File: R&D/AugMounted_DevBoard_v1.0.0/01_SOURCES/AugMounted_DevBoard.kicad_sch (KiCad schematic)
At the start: 0 parts

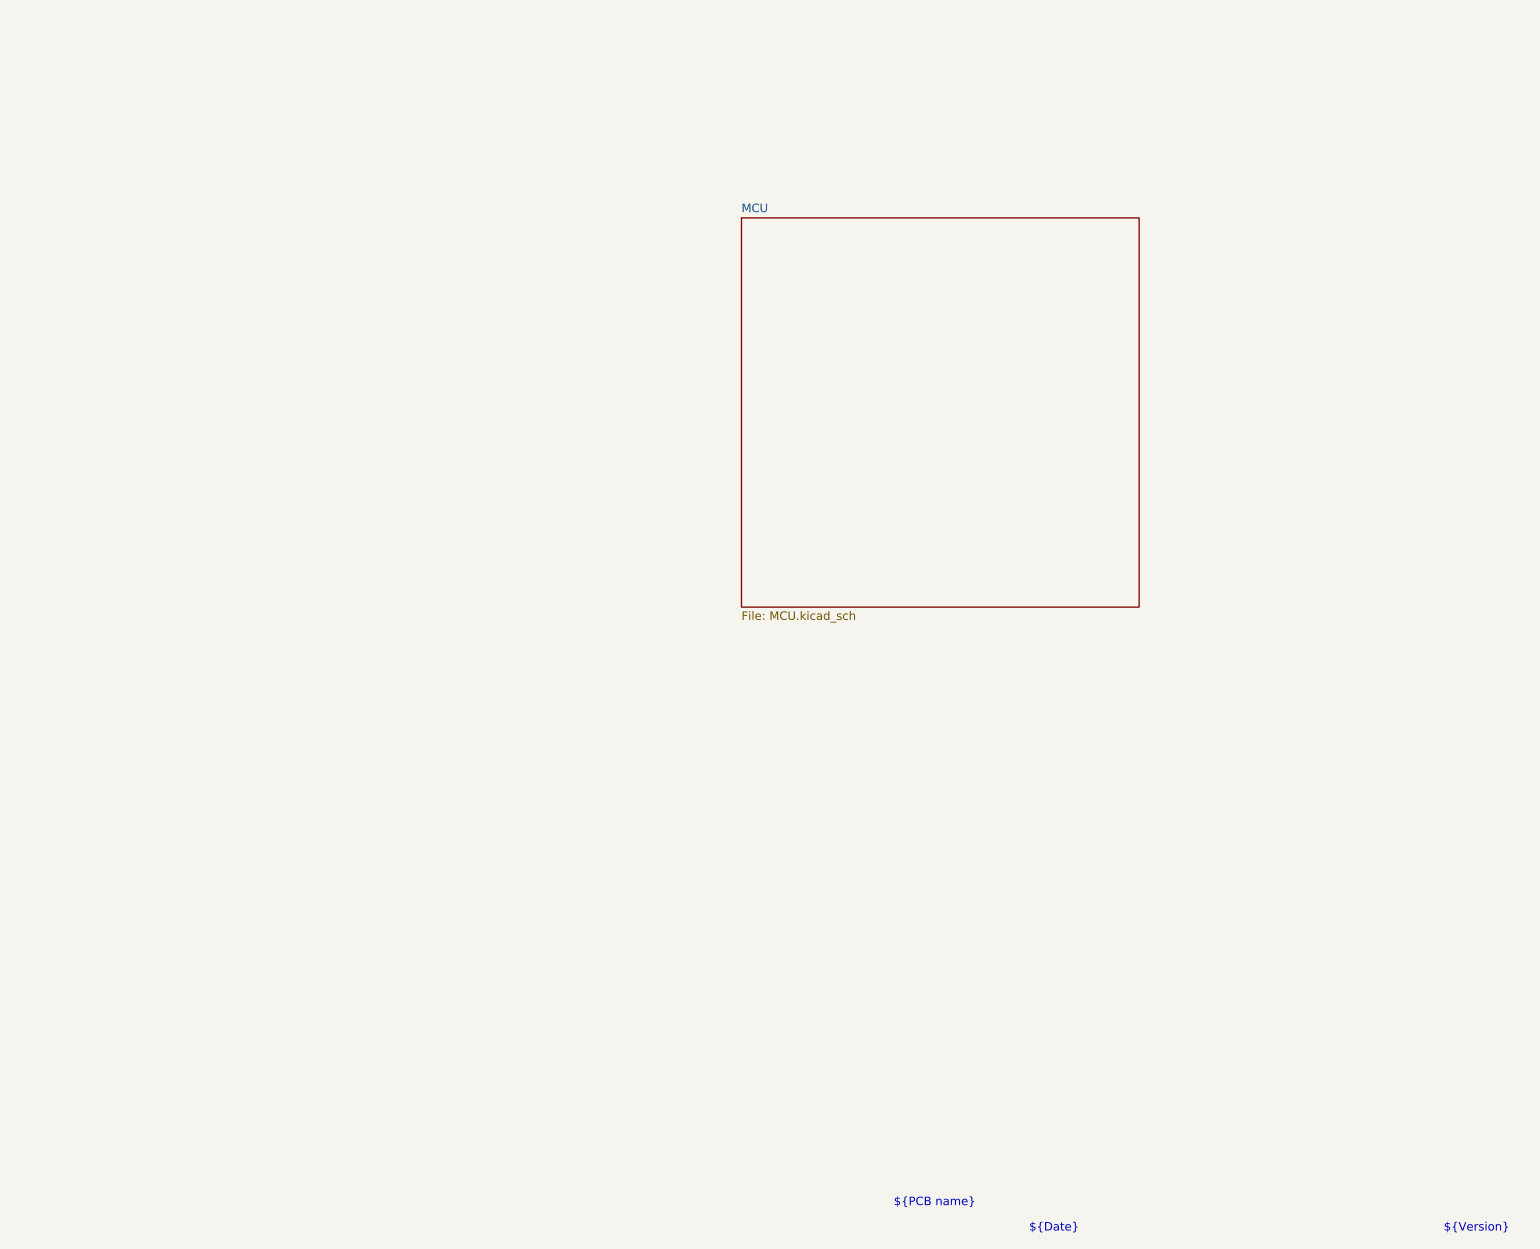
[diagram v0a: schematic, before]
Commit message: Created all components, placed them, and added images of typical applications. ECX334A and ESP32-S3 pdf are available in 00_RESOURCES
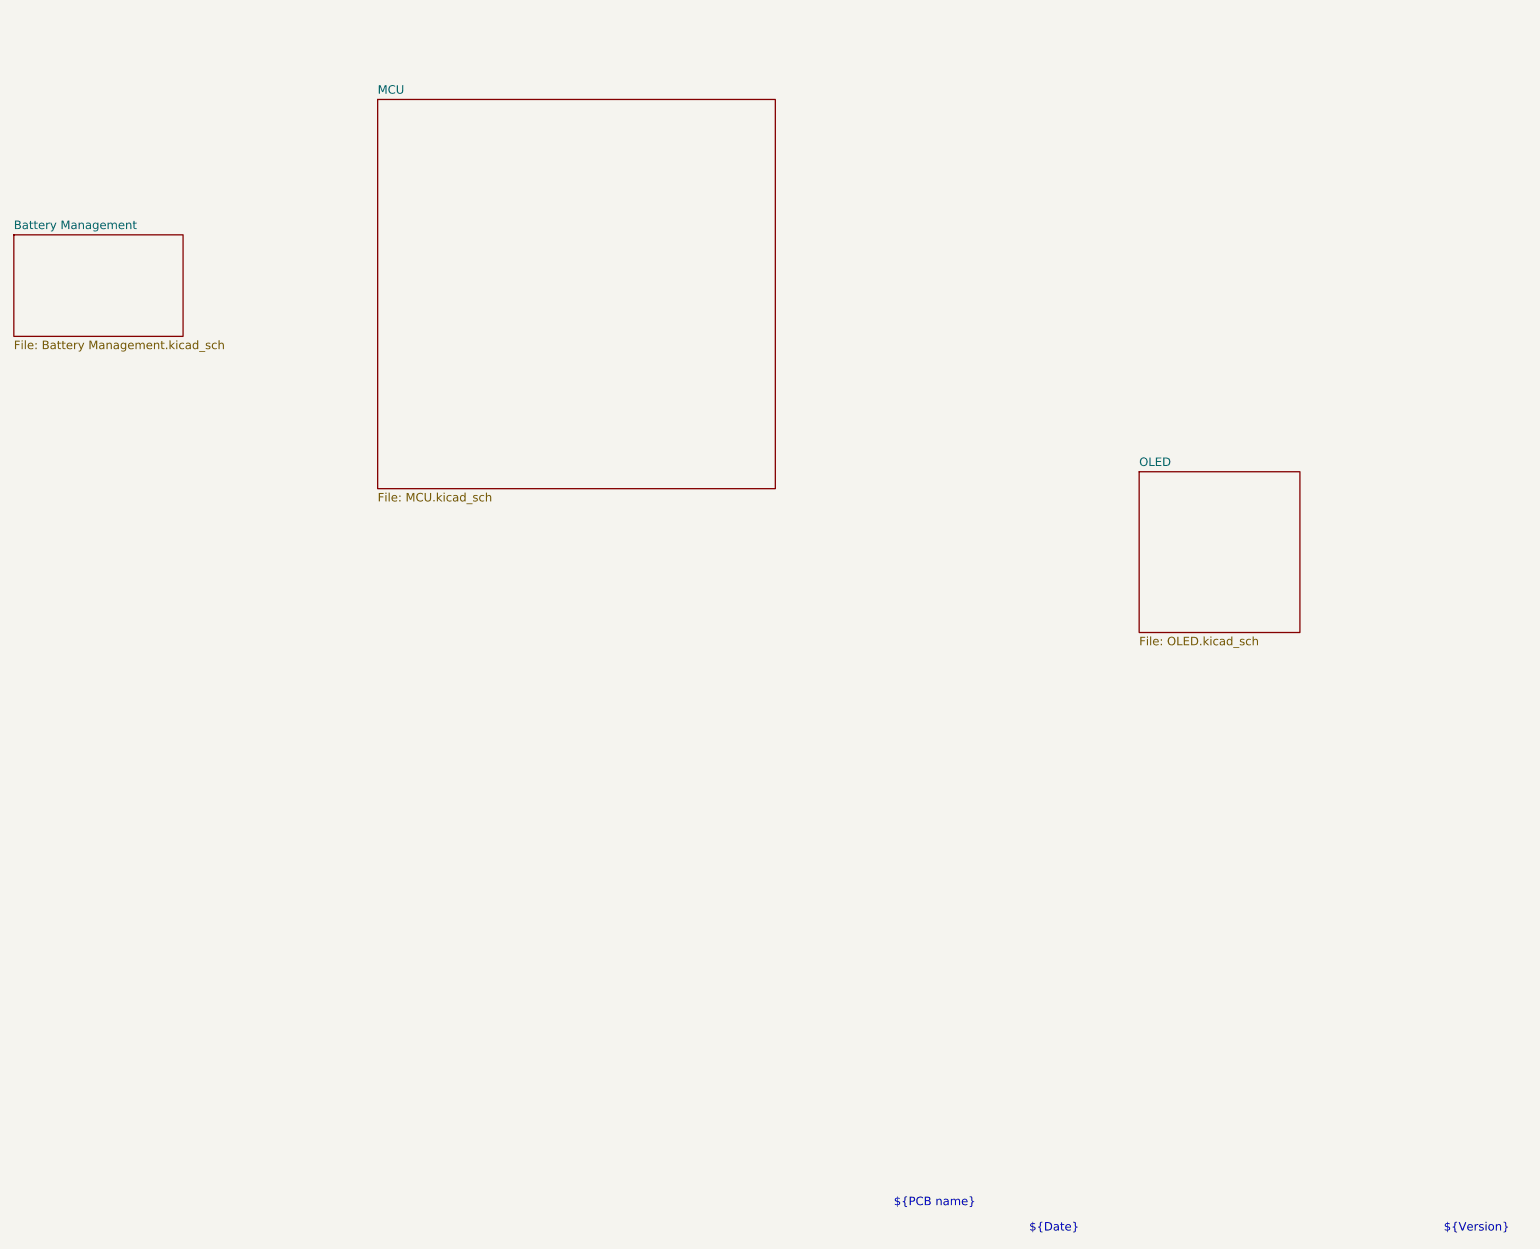
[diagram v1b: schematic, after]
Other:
- added sheet Battery Management (Battery Management.kicad_sch)
- added sheet OLED (OLED.kicad_sch)
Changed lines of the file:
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@@
     (effects (font (size 1.27 1.27)) (justify left bottom))
   )
-  (sheet (at 163.83 41.91) (size 59.69 58.42) (fields_autoplaced)
+  (sheet (at 54.61 44.45) (size 25.4 15.24) (fields_autoplaced)
     (stroke (width 0.1524) (type solid))
     (fill (color 0 0 0 0.0000))
-    (property "Sheetname" "MCU" (at 163.83 41.1984 0)
+    (property "Sheetname" "Battery Management" (at 54.61 43.7384 0)
       (effects (font (size 1.27 1.27)) (justify left bottom))
     )
-    (property "Sheetfile" "MCU.kicad_sch" (at 163.83 100.9146 0)
+    (property "Sheetfile" "Battery Management.kicad_sch" (at 54.61 60.2746 0)
       (effects (font (size 1.27 1.27)) (justify left top))
     )
+    (instances
+      (project "AugMounted_DevBoard"
+        (path "/75b08848-9393-425e-a17d-60105119a7b1" (page "3"))
+      )
+    )
+  )
+  (sheet (at 223.52 80.01) (size 24.13 24.13) (fields_autoplaced)
+    (stroke (width 0.1524) (type solid))
+    (fill (color 0 0 0 0.0000))
+    (property "Sheetname" "OLED" (at 223.52 79.2984 0)
+      (effects (font (size 1.27 1.27)) (justify left bottom))
+    )
+    (property "Sheetfile" "OLED.kicad_sch" (at 223.52 104.7246 0)
+      (effects (font (size 1.27 1.27)) (justify left top))
+    )
+    (instances
+      (project "AugMounted_DevBoard"
+        (path "/75b08848-9393-425e-a17d-60105119a7b1" (page "4"))
+      )
+    )
+  )
+  (sheet (at 109.22 24.13) (size 59.69 58.42) (fields_autoplaced)
+    (stroke (width 0.1524) (type solid))
+    (fill (color 0 0 0 0.0000))
+    (property "Sheetname" "MCU" (at 109.22 23.4184 0)
+      (effects (font (size 1.27 1.27)) (justify left bottom))
+    )
+    (property "Sheetfile" "MCU.kicad_sch" (at 109.22 83.1346 0)
+      (effects (font (size 1.27 1.27)) (justify left top))
+    )

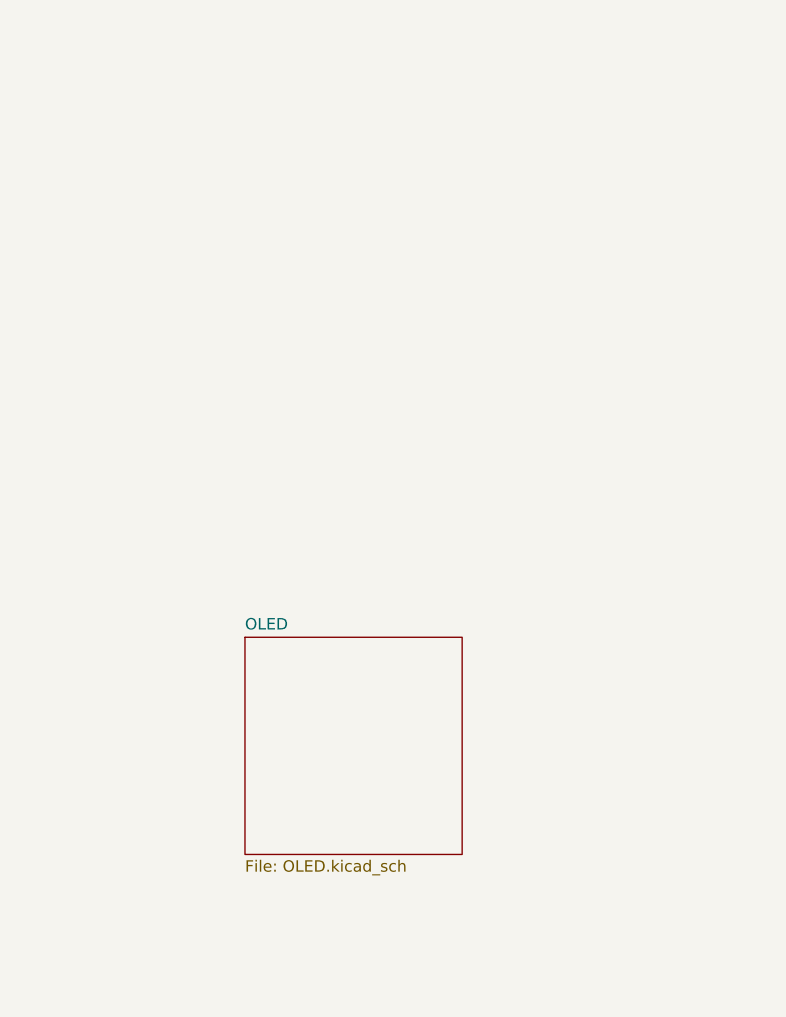
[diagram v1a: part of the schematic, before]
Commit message: Oled driving circuit done, need to connect everything to the ESP32
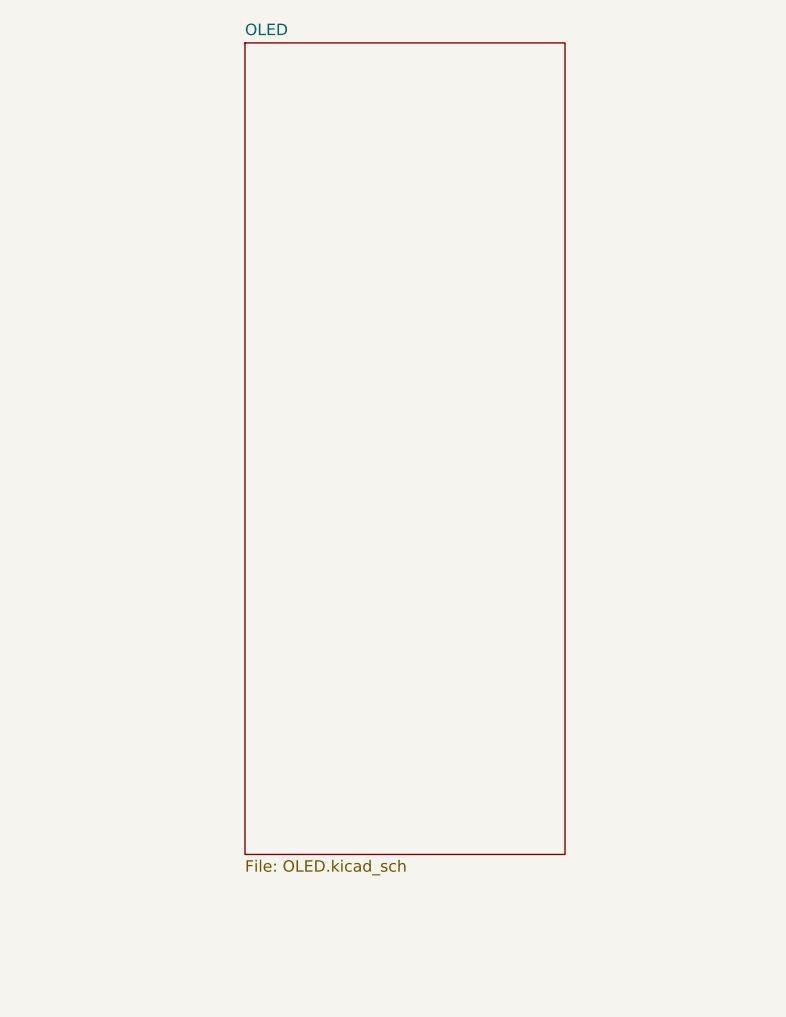
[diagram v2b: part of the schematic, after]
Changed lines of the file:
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@@
     )
   )
-  (sheet (at 223.52 80.01) (size 24.13 24.13) (fields_autoplaced)
+  (sheet (at 223.52 13.97) (size 35.56 90.17) (fields_autoplaced)
     (stroke (width 0.1524) (type solid))
     (fill (color 0 0 0 0.0000))
-    (property "Sheetname" "OLED" (at 223.52 79.2984 0)
+    (property "Sheetname" "OLED" (at 223.52 13.2584 0)
       (effects (font (size 1.27 1.27)) (justify left bottom))
     )

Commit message: Schematic 90% done
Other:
- added sheet User Input (User Input.kicad_sch)
- sheet Battery Management ports: added 1.8V_ENABLE, 1.8V_LCD, 10V_ENABLE, BUTTON_PIN, ENCODER_S1, ENCODER_S2, ESP_ENCODER_BUTTON_PIN, ESP_POWER_EN, SCL, SDA; removed none
- sheet MCU ports: added B1, B2, B3, B4, B5, CS, ESP_POWER_EN, G1, G2, G3, G4, G5, G6, HVD, MCLK, MISO, MOSI, R1, R2, R3, R4, R5, SCK, SCL, SDA, XCLR, XHD; removed none
- sheet OLED ports: added 1.8V_LCD, B1, B2, B3, B4, B5, CS, G1, G2, G3, G4, G5, G6, HVD, MCLK, MISO, MOSI, R1, R2, R3, R4, R5, RGB_LSB, SCK, XCLR, XHD; removed none

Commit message: Moved components
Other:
- sheet MCU ports: added ENCODER_S1, ENCODER_S2; removed none
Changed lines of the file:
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@@
     (effects (font (size 1.27 1.27)) (justify right))
   )
-  (label "ENCODER_S2" (at 129.54 130.81 0) (fields_autoplaced)
+  (label "ENCODER_S2" (at 100.33 124.46 0) (fields_autoplaced)
     (effects (font (size 1.27 1.27)) (justify left bottom))
   )
@@
     (effects (font (size 1.27 1.27)) (justify right))
   )
-  (label "ENCODER_S1" (at 129.54 128.27 0) (fields_autoplaced)
+  (label "ENCODER_S1" (at 100.33 121.92 0) (fields_autoplaced)
     (effects (font (size 1.27 1.27)) (justify left bottom))
   )
@@
     (effects (font (size 1.27 1.27)) (justify right bottom))
   )
+  (label "ENCODER_S1" (at 154.94 85.09 180) (fields_autoplaced)
+    (effects (font (size 1.27 1.27)) (justify right bottom))
+  )
   (label "XHD" (at 220.98 96.52 180) (fields_autoplaced)
     (effects (font (size 1.27 1.27)) (justify right))
   )
-  (label "ENCODER_A" (at 129.54 123.19 0) (fields_autoplaced)
+  (label "ENCODER_A" (at 100.33 116.84 0) (fields_autoplaced)
     (effects (font (size 1.27 1.27)) (justify left bottom))
   )
@@
     (effects (font (size 1.27 1.27)) (justify right))
   )
+  (label "ENCODER_S2" (at 154.94 87.63 180) (fields_autoplaced)
+    (effects (font (size 1.27 1.27)) (justify right bottom))
+  )
   (label "B4" (at 220.98 58.42 180) (fields_autoplaced)
     (effects (font (size 1.27 1.27)) (justify right))
@@
     (effects (font (size 1.27 1.27)) (justify right))
   )
-  (label "ENCODER_B" (at 129.54 125.73 0) (fields_autoplaced)
+  (label "ENCODER_B" (at 100.33 119.38 0) (fields_autoplaced)
     (effects (font (size 1.27 1.27)) (justify left bottom))
   )
@@
     (effects (font (size 1.27 1.27)) (justify left bottom))
   )
-  (sheet (at 106.68 120.65) (size 22.86 15.24) (fields_autoplaced)
+  (sheet (at 77.47 114.3) (size 22.86 15.24) (fields_autoplaced)
     (stroke (width 0.1524) (type solid))
     (fill (color 0 0 0 0.0000))
-    (property "Sheetname" "User Input" (at 106.68 119.9384 0)
+    (property "Sheetname" "User Input" (at 77.47 113.5884 0)
       (effects (font (size 1.27 1.27)) (justify left bottom))
     )
-    (property "Sheetfile" "User Input.kicad_sch" (at 106.68 136.4746 0)
+    (property "Sheetfile" "User Input.kicad_sch" (at 77.47 130.1246 0)
       (effects (font (size 1.27 1.27)) (justify left top))
     )
-    (pin "ENCODER_A" output (at 129.54 123.19 0)
-      (effects (font (size 1.27 1.27)) (justify right))
-    )
-    (pin "ENCODER_B" output (at 129.54 125.73 0)
-      (effects (font (size 1.27 1.27)) (justify right))
-    )
-    (pin "ENCODER_S2" output (at 129.54 130.81 0)
-      (effects (font (size 1.27 1.27)) (justify right))
-    )
-    (pin "ENCODER_S1" output (at 129.54 128.27 0)
+    (pin "ENCODER_A" output (at 100.33 116.84 0)
+      (effects (font (size 1.27 1.27)) (justify right))
+    )
+    (pin "ENCODER_B" output (at 100.33 119.38 0)
+      (effects (font (size 1.27 1.27)) (justify right))
+    )
+    (pin "ENCODER_S2" output (at 100.33 124.46 0)
+      (effects (font (size 1.27 1.27)) (justify right))
+    )
+    (pin "ENCODER_S1" output (at 100.33 121.92 0)
       (effects (font (size 1.27 1.27)) (justify right))
     )
@@
       (effects (font (size 1.27 1.27)) (justify left))
     )
+    (pin "ENCODER_S1" input (at 154.94 85.09 180)
+      (effects (font (size 1.27 1.27)) (justify left))
+    )
+    (pin "ENCODER_S2" input (at 154.94 87.63 180)
+      (effects (font (size 1.27 1.27)) (justify left))
+    )
